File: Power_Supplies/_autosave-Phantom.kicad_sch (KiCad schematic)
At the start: 20 parts, among them IC2 LT8338, U37 PEC11R-4030F-N0024, U38 Si5351A-B-GT, X3 FA-238 24.0000MB-C0 (CRYSTAL)

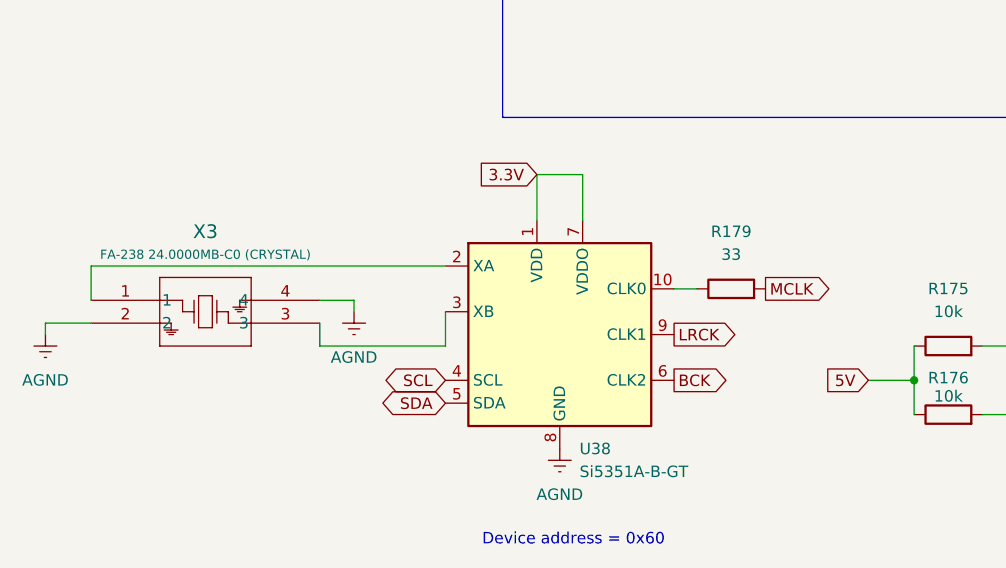
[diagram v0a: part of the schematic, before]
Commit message: Added BIG KNOB schematic and started PCB
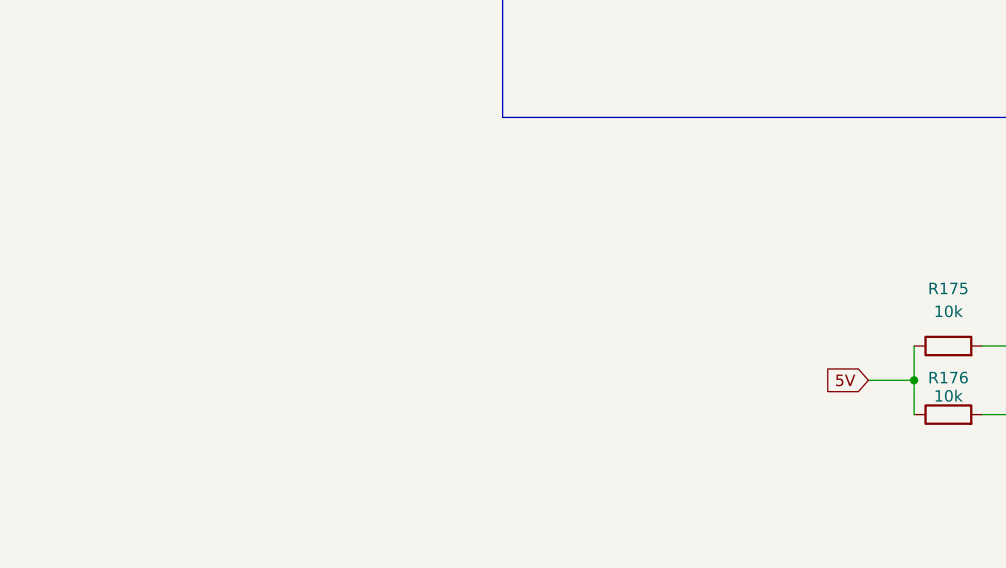
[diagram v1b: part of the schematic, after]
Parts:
- removed R179: 33, Resistor_SMD:R_0805_2012Metric, symbol Device:R
- removed U38: Si5351A-B-GT, Package_SO:MSOP-10_3x3mm_P0.5mm, symbol Oscillator:Si5351A-B-GT
- removed X3: FA-238 24.0000MB-C0 (CRYSTAL), SamacSys_Parts:FA-238_EPS, symbol SDLibrary:FA-238_24.0000MB-C0
- IC2: footprint SamacSys_Parts:SOP65P490X110-9N -> SamacSys_Parts:SOP50P490X110-11N
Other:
- note removed: "Device address = 0x60"
